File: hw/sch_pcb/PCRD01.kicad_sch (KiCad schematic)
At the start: 40 parts, among them J1 JUMP_3X2, J2 JUMP_5X2, J3 CONN1_2, J4 CONN1_2, J5 Out, P1 _, P2 _, P3 _, P4 _, Q1 BF862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

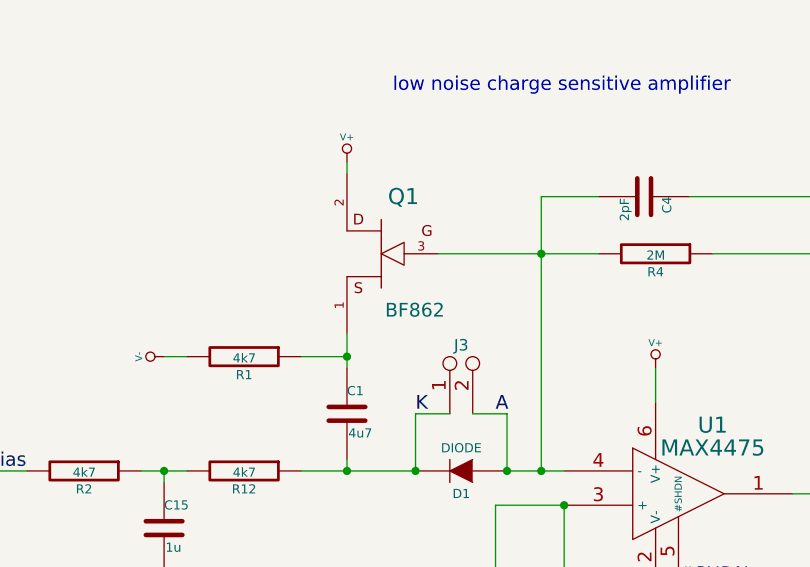
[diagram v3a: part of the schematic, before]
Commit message: replace PCB capacitor
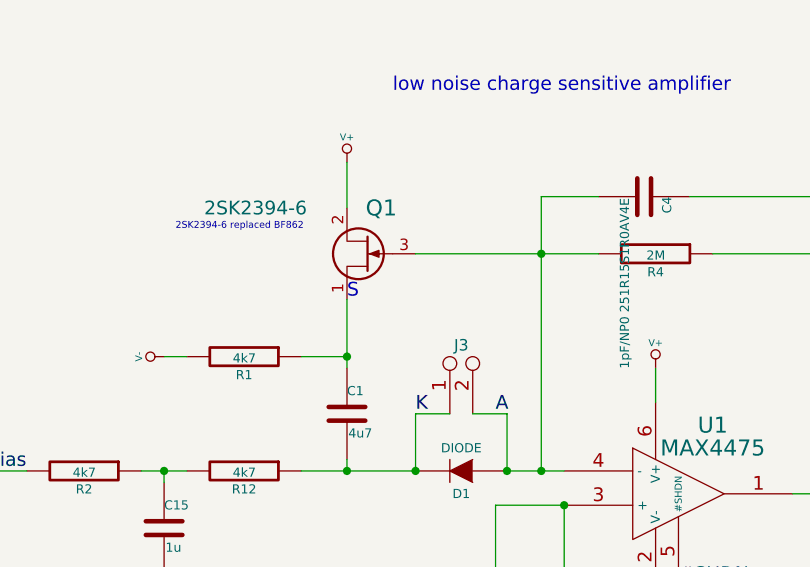
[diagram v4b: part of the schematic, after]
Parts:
- C4: value 2pF -> 1pF/NP0 251R15S1R0AV4E; footprint (none) -> Mlab_R:SMD-0805; UST_ID (none) -> 5c70984712875079b91f8b9f
- Q1: value BF862 -> 2SK2394-6; footprint MLAB_IO:SOT-23 -> Package_TO_SOT_SMD:SOT-23; symbol PCRD01A-rescue:JFET_N -> Transistor_FET:BF545A; UST_ID (none) -> 628d134fdc56076e9a223625
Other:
- note added: "2SK2394-6 replaced BF862"
- note added: "S"
- moved on the sheet: Q1
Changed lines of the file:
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@@
-    (stroke (width 0) (type default) (color 0 0 0 0))
-  )
-  (wire (pts (xy 63.5 67.31) (xy 63.5 66.04))
     (stroke (width 0) (type default) (color 0 0 0 0))
   )
@@
     (stroke (width 0) (type default) (color 0 0 0 0))
   )
-  (wire (pts (xy 73.66 76.2) (xy 85.09 76.2))
+  (wire (pts (xy 71.12 76.2) (xy 85.09 76.2))
     (stroke (width 0) (type default) (color 0 0 0 0))
   )
@@
     (stroke (width 0) (type default) (color 0 0 0 0))
   )
+  (wire (pts (xy 63.5 66.04) (xy 63.5 71.12))
+    (stroke (width 0) (type default) (color 0 0 0 0))
+  )
   (wire (pts (xy 58.42 87.63) (xy 63.5 87.63))
     (stroke (width 0) (type default) (color 0 0 0 0))
@@
     (stroke (width 0) (type default) (color 0 0 0 0))
   )
-  (wire (pts (xy 63.5 85.09) (xy 63.5 87.63))
+  (wire (pts (xy 63.5 81.28) (xy 63.5 87.63))
     (stroke (width 0) (type default) (color 0 0 0 0))
   )
@@
     (effects (font (size 1.524 1.524)) (justify left bottom))
   )
+  (text "S" (at 63.5 81.28 0)
+    (effects (font (size 1.524 1.524)) (justify left bottom))
+  )
   (text "+/- 2,4V" (at 38.1 154.94 0)
     (effects (font (size 1.524 1.524)) (justify left bottom))
@@
   (text "amplifier 7,7x" (at 152.4 86.36 0)
     (effects (font (size 1.524 1.524)) (justify left bottom))
+  )
+  (text "2SK2394-6 replaced BF862" (at 44.45 73.66 0)
+    (effects (font (size 0.762 0.762)) (justify left bottom))
   )
   (text "low noise charge sensitive amplifier" (at 68.58 58.42 0)
@@
     (pin "2")
   )
-  (symbol (lib_id "PCRD01A-rescue:JFET_N") (at 67.31 76.2 0) (mirror y) (unit 1)
-    (in_bom yes) (on_board yes)
-    (property "Reference" "Q1" (id 0) (at 69.7738 69.85 0)
+  (symbol (lib_id "Transistor_FET:BF545A") (at 66.04 76.2 0) (mirror y) (unit 1)
+    (in_bom yes) (on_board yes)
+    (property "Reference" "Q1" (id 0) (at 67.31 71.12 0)
       (effects (font (size 1.778 1.778)))
     )
-    (property "Value" "BF862" (id 1) (at 71.0438 82.4738 0)
-      (effects (font (size 1.524 1.524)))
-    )
-    (property "Footprint" "MLAB_IO:SOT-23" (id 2) (at 67.31 76.2 0)
-      (effects (font (size 1.524 1.524)) hide)
-    )
-    (property "Datasheet" "" (id 3) (at 67.31 76.2 0)
-      (effects (font (size 1.524 1.524)))
+    (property "Value" "2SK2394-6" (id 1) (at 53.34 71.12 0)
+      (effects (font (size 1.524 1.524)))
+    )
+    (property "Footprint" "Package_TO_SOT_SMD:SOT-23" (id 2) (at 60.96 78.105 0)
+      (effects (font (size 1.27 1.27) italic) (justify left) hide)
+    )
+    (property "Datasheet" "https://www.nxp.com/docs/en/data-sheet/BF545A_BF545B_BF545C.pdf" (id 3) (at 66.04 76.2 0)
+      (effects (font (size 1.27 1.27)) (justify left) hide)
+    )
+    (property "UST_ID" "628d134fdc56076e9a223625" (id 4) (at 66.04 76.2 0)
+      (effects (font (size 1.27 1.27)) hide)
     )
     (pin "1")
@@
       (effects (font (size 1.016 1.016)) (justify left))
     )
-    (property "Value" "2pF" (id 1) (at 94.361 70.0024 0)
-      (effects (font (size 1.016 1.016)) (justify left))
-    )
-    (property "Footprint" "" (id 2) (at 92.71 70.8152 0)
+    (property "Value" "1pF/NP0 251R15S1R0AV4E" (id 1) (at 94.361 70.0024 0)
+      (effects (font (size 1.016 1.016)) (justify left))
+    )
+    (property "Footprint" "Mlab_R:SMD-0805" (id 2) (at 92.71 70.8152 0)
       (effects (font (size 0.762 0.762)) hide)
     )
     (property "Datasheet" "" (id 3) (at 96.52 69.85 0)
       (effects (font (size 1.524 1.524)))
+    )
+    (property "UST_ID" "5c70984712875079b91f8b9f" (id 4) (at 96.52 69.85 0)
+      (effects (font (size 1.27 1.27)) hide)
     )
     (pin "1")
@@
     )
     (path "/00000000-0000-0000-0000-0000547638f8"
-      (reference "C4") (unit 1) (value "2pF") (footprint "")
+      (reference "C4") (unit 1) (value "1pF/NP0 251R15S1R0AV4E") (footprint "Mlab_R:SMD-0805")
     )
     (path "/00000000-0000-0000-0000-00005483ba04"
@@
     )
     (path "/00000000-0000-0000-0000-000054763801"
-      (reference "Q1") (unit 1) (value "BF862") (footprint "MLAB_IO:SOT-23")
+      (reference "Q1") (unit 1) (value "2SK2394-6") (footprint "Package_TO_SOT_SMD:SOT-23")
     )
     (path "/00000000-0000-0000-0000-0000547633b6"

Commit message: uklid layoutu
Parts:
- removed J3: CONN1_2, Hrebinky:CONN_3_2, symbol PCRD01A-rescue:CONN1_2
- added J3: HEADER_1x03, Mlab_Pin_Headers:Straight_1x03, symbol MLAB_HEADER:HEADER_1x03
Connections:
- net A: now also J3.3
- net GND: now also J3.2
- net K: now also J3.1
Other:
- note added: "Originaly: PCB 2pF capacitor"
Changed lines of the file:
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@@
     (stroke (width 0) (type default) (color 0 0 0 0))
   )
-  (wire (pts (xy 71.12 93.98) (xy 74.93 93.98))
+  (wire (pts (xy 71.12 93.98) (xy 73.66 93.98))
     (stroke (width 0) (type default) (color 0 0 0 0))
   )
@@
     (stroke (width 0) (type default) (color 0 0 0 0))
   )
+  (wire (pts (xy 78.74 93.98) (xy 81.28 93.98))
+    (stroke (width 0) (type default) (color 0 0 0 0))
+  )
   (wire (pts (xy 113.03 102.87) (xy 115.57 102.87))
     (stroke (width 0) (type default) (color 0 0 0 0))
@@
     (stroke (width 0) (type default) (color 0 0 0 0))
   )
+  (wire (pts (xy 73.66 88.9) (xy 73.66 93.98))
+    (stroke (width 0) (type default) (color 0 0 0 0))
+  )
   (wire (pts (xy 261.62 26.67) (xy 261.62 30.48))
     (stroke (width 0) (type default) (color 0 0 0 0))
@@
     (stroke (width 0) (type default) (color 0 0 0 0))
   )
-  (wire (pts (xy 77.47 93.98) (xy 81.28 93.98))
-    (stroke (width 0) (type default) (color 0 0 0 0))
-  )
   (wire (pts (xy 267.97 102.87) (xy 270.51 102.87))
     (stroke (width 0) (type default) (color 0 0 0 0))
@@
   )
   (wire (pts (xy 43.18 165.1) (xy 43.18 170.18))
+    (stroke (width 0) (type default) (color 0 0 0 0))
+  )
+  (wire (pts (xy 78.74 88.9) (xy 78.74 93.98))
     (stroke (width 0) (type default) (color 0 0 0 0))
   )
@@
   (text "amplifier 7,7x" (at 152.4 86.36 0)
     (effects (font (size 1.524 1.524)) (justify left bottom))
+  )
+  (text "Originaly: PCB 2pF capacitor" (at 90.17 64.77 0)
+    (effects (font (size 0.762 0.762)) (justify left bottom))
   )
   (text "2SK2394-6 replaced BF862" (at 44.45 73.66 0)
@@
       (effects (font (size 1.016 1.016)) (justify left))
     )
-    (property "Value" "1pF/NP0 251R15S1R0AV4E" (id 1) (at 94.361 70.0024 0)
+    (property "Value" "1pF/NP0 251R15S1R0AV4E" (id 1) (at 90.17 66.04 90)
       (effects (font (size 1.016 1.016)) (justify left))
     )
@@
     (pin "1")
   )
-  (symbol (lib_id "PCRD01A-rescue:CONN1_2") (at 76.2 86.36 90) (unit 1)
-    (in_bom yes) (on_board yes)
-    (property "Reference" "J3" (id 0) (at 76.2 86.36 90))
-    (property "Value" "CONN1_2" (id 1) (at 77.47 83.82 0)
-      (effects (font (size 1.016 1.016)) hide)
-    )
-    (property "Footprint" "Hrebinky:CONN_3_2" (id 2) (at 77.47 85.09 0)
+  (symbol (lib_id "PCRD01A-rescue:V+") (at 105.41 116.84 0) (unit 1)
+    (in_bom yes) (on_board yes)
+    (property "Reference" "#PWR031" (id 0) (at 105.41 114.3 0)
+      (effects (font (size 0.762 0.762)) hide)
+    )
+    (property "Value" "V+" (id 1) (at 105.41 114.046 0)
+      (effects (font (size 0.762 0.762)))
+    )
+    (property "Footprint" "" (id 2) (at 105.41 116.84 0)
+      (effects (font (size 1.524 1.524)))
+    )
+    (property "Datasheet" "" (id 3) (at 105.41 116.84 0)
+      (effects (font (size 1.524 1.524)))
+    )
+    (pin "1")
+  )
+  (symbol (lib_id "PCRD01A-rescue:R") (at 52.07 100.33 270) (unit 1)
+    (in_bom yes) (on_board yes)
+    (property "Reference" "R12" (id 0) (at 52.07 102.362 90)
+      (effects (font (size 1.016 1.016)))
+    )
+    (property "Value" "4k7" (id 1) (at 52.0954 100.5078 90)
+      (effects (font (size 1.016 1.016)))
+    )
+    (property "Footprint" "Mlab_R:SMD-0805" (id 2) (at 52.07 98.552 90)
+      (effects (font (size 0.762 0.762)) hide)
+    )
+    (property "Datasheet" "" (id 3) (at 52.07 100.33 0)
+      (effects (font (size 0.762 0.762)))
+    )
+    (property "UST_ID" "5c70984612875079b91f8995" (id 4) (at 52.07 100.33 0)
+      (effects (font (size 1.27 1.27)) hide)
+    )
+    (pin "1")
+    (pin "2")
+  )
+  (symbol (lib_id "PCRD01A-rescue:C") (at 43.18 106.68 0) (unit 1)
+    (in_bom yes) (on_board yes)
+    (property "Reference" "C15" (id 0) (at 43.18 104.14 0)
+      (effects (font (size 1.016 1.016)) (justify left))
+    )
+    (property "Value" "1u" (id 1) (at 43.3324 108.839 0)
+      (effects (font (size 1.016 1.016)) (justify left))
+    )
+    (property "Footprint" "Mlab_R:SMD-0805" (id 2) (at 44.1452 110.49 0)
+      (effects (font (size 0.762 0.762)) hide)
+    )
+    (property "Datasheet" "" (id 3) (at 43.18 106.68 0)
+      (effects (font (size 1.524 1.524)))
+    )
+    (property "UST_ID" "5c70984712875079b91f8b50" (id 4) (at 43.18 106.68 0)
+      (effects (font (size 1.27 1.27)) hide)
+    )
+    (pin "1")
+    (pin "2")
+  )
+  (symbol (lib_id "PCRD01A-rescue:GND") (at 43.18 113.03 0) (unit 1)
+    (in_bom yes) (on_board yes)
+    (property "Reference" "#PWR032" (id 0) (at 43.18 113.03 0)
+      (effects (font (size 0.762 0.762)) hide)
+    )
+    (property "Value" "GND" (id 1) (at 43.18 114.808 0)
+      (effects (font (size 0.762 0.762)) hide)
+    )
+    (property "Footprint" "" (id 2) (at 43.18 113.03 0)
+      (effects (font (size 1.524 1.524)))
+    )
+    (property "Datasheet" "" (id 3) (at 43.18 113.03 0)
+      (effects (font (size 1.524 1.524)))
+    )
+    (pin "1")
+  )
+  (symbol (lib_id "PCRD01A-rescue:GND") (at 76.2 88.9 0) (unit 1)
+    (in_bom yes) (on_board yes)
+    (property "Reference" "#PWR0101" (id 0) (at 76.2 88.9 0)
+      (effects (font (size 0.762 0.762)) hide)
+    )
+    (property "Value" "GND" (id 1) (at 76.2 90.678 0)
+      (effects (font (size 0.762 0.762)) hide)
+    )
+    (property "Footprint" "" (id 2) (at 76.2 88.9 0)
+      (effects (font (size 1.524 1.524)))
+    )
+    (property "Datasheet" "" (id 3) (at 76.2 88.9 0)
+      (effects (font (size 1.524 1.524)))
+    )
+    (pin "1")
+  )
+  (symbol (lib_id "MLAB_HEADER:HEADER_1x03") (at 76.2 83.82 90) (unit 1)
+    (in_bom yes) (on_board yes) (fields_autoplaced)
+    (property "Reference" "J3" (id 0) (at 81.28 84.455 90)
+      (effects (font (size 1.524 1.524)) (justify right))
+    )
+    (property "Value" "HEADER_1x03" (id 1) (at 81.28 86.36 90)
+      (effects (font (size 1.524 1.524)) (justify right) hide)
+    )
+    (property "Footprint" "Mlab_Pin_Headers:Straight_1x03" (id 2) (at 73.66 83.82 0)
       (effects (font (size 1.524 1.524)) hide)
     )
-    (property "Datasheet" "" (id 3) (at 77.47 85.09 0)
-      (effects (font (size 1.524 1.524)))
-    )
-    (pin "1")
-    (pin "2")
-  )
-  (symbol (lib_id "PCRD01A-rescue:V+") (at 105.41 116.84 0) (unit 1)
-    (in_bom yes) (on_board yes)
-    (property "Reference" "#PWR031" (id 0) (at 105.41 114.3 0)
-      (effects (font (size 0.762 0.762)) hide)
-    )
-    (property "Value" "V+" (id 1) (at 105.41 114.046 0)
-      (effects (font (size 0.762 0.762)))
-    )
-    (property "Footprint" "" (id 2) (at 105.41 116.84 0)
-      (effects (font (size 1.524 1.524)))
-    )
-    (property "Datasheet" "" (id 3) (at 105.41 116.84 0)
-      (effects (font (size 1.524 1.524)))
-    )
-    (pin "1")
-  )
-  (symbol (lib_id "PCRD01A-rescue:R") (at 52.07 100.33 270) (unit 1)
-    (in_bom yes) (on_board yes)
-    (property "Reference" "R12" (id 0) (at 52.07 102.362 90)
-      (effects (font (size 1.016 1.016)))
-    )
-    (property "Value" "4k7" (id 1) (at 52.0954 100.5078 90)
-      (effects (font (size 1.016 1.016)))
-    )
-    (property "Footprint" "Mlab_R:SMD-0805" (id 2) (at 52.07 98.552 90)
-      (effects (font (size 0.762 0.762)) hide)
-    )
-    (property "Datasheet" "" (id 3) (at 52.07 100.33 0)
-      (effects (font (size 0.762 0.762)))
-    )
-    (property "UST_ID" "5c70984612875079b91f8995" (id 4) (at 52.07 100.33 0)
-      (effects (font (size 1.27 1.27)) hide)
-    )
-    (pin "1")
-    (pin "2")
-  )
-  (symbol (lib_id "PCRD01A-rescue:C") (at 43.18 106.68 0) (unit 1)
-    (in_bom yes) (on_board yes)
-    (property "Reference" "C15" (id 0) (at 43.18 104.14 0)
-      (effects (font (size 1.016 1.016)) (justify left))
-    )
-    (property "Value" "1u" (id 1) (at 43.3324 108.839 0)
-      (effects (font (size 1.016 1.016)) (justify left))
-    )
-    (property "Footprint" "Mlab_R:SMD-0805" (id 2) (at 44.1452 110.49 0)
-      (effects (font (size 0.762 0.762)) hide)
-    )
-    (property "Datasheet" "" (id 3) (at 43.18 106.68 0)
-      (effects (font (size 1.524 1.524)))
-    )
-    (property "UST_ID" "5c70984712875079b91f8b50" (id 4) (at 43.18 106.68 0)
-      (effects (font (size 1.27 1.27)) hide)
-    )
-    (pin "1")
-    (pin "2")
-  )
-  (symbol (lib_id "PCRD01A-rescue:GND") (at 43.18 113.03 0) (unit 1)
-    (in_bom yes) (on_board yes)
-    (property "Reference" "#PWR032" (id 0) (at 43.18 113.03 0)
-      (effects (font (size 0.762 0.762)) hide)
-    )
-    (property "Value" "GND" (id 1) (at 43.18 114.808 0)
-      (effects (font (size 0.762 0.762)) hide)
-    )
-    (property "Footprint" "" (id 2) (at 43.18 113.03 0)
-      (effects (font (size 1.524 1.524)))
-    )
-    (property "Datasheet" "" (id 3) (at 43.18 113.03 0)
-      (effects (font (size 1.524 1.524)))
-    )
-    (pin "1")
+    (property "Datasheet" "" (id 3) (at 73.66 83.82 0)
+      (effects (font (size 1.524 1.524)))
+    )
+    (pin "1")
+    (pin "2")
+    (pin "3")
   )
   (sheet_instances
@@
       (reference "#PWR032") (unit 1) (value "GND") (footprint "")
     )
+    (path "/4c66d86a-55d0-4bc7-9f02-eebc8b70e762"
+      (reference "#PWR0101") (unit 1) (value "GND") (footprint "")
+    )
     (path "/00000000-0000-0000-0000-00005476354e"
       (reference "C1") (unit 1) (value "4u7") (footprint "Mlab_R:SMD-0805")
@@
       (reference "J2") (unit 1) (value "JUMP_5X2") (footprint "Hrebinky:Pin_Header_Straight_2x05")
     )
-    (path "/00000000-0000-0000-0000-0000548463a5"
-      (reference "J3") (unit 1) (value "CONN1_2") (footprint "Hrebinky:CONN_3_2")
+    (path "/bd4f2901-c4b7-4421-b66c-d0d47ad8871a"
+      (reference "J3") (unit 1) (value "HEADER_1x03") (footprint "Mlab_Pin_Headers:Straight_1x03")
     )
     (path "/00000000-0000-0000-0000-00005483ad5f"

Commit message: Edit PCB
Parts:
- C1, C10, C11, C12, C13, C15, C2, C3, C4, C5, C6, C7, C8, C9: footprint Mlab_R:SMD-0805 -> Capacitor_SMD:C_0805_2012Metric
- C14: footprint MLAB_R:SMD-0805 -> Capacitor_SMD:C_0805_2012Metric
- J1, J5: footprint Hrebinky:Pin_Header_Straight_2x03 -> Mlab_Pin_Headers:Straight_2x03; symbol PCRD01A-rescue:JUMP_3X2 -> MLAB_HEADER:HEADER_2x03_PARALLEL
- J2: footprint Hrebinky:Pin_Header_Straight_2x05 -> Mlab_Pin_Headers:Straight_2x05; symbol PCRD01A-rescue:JUMP_5X2 -> MLAB_HEADER:HEADER_2x05_PARALLEL
- J4: footprint Hrebinky:Pin_Header_Straight_1x02 -> Mlab_Pin_Headers:Straight_1x02
- R1, R10, R11, R12, R2, R3, R4, R5, R6, R7, R8, R9: footprint Mlab_R:SMD-0805 -> Resistor_SMD:R_0805_2012Metric
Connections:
- net +Ubias: now also J1.3, J1.4; no longer J1.2 (1), J1.5
- net GND: now also J1.2, J1.5, J2.2, J2.9, J5.2, J5.5; no longer J1.3, J1.4, J2.5, J2.6, J5.3, J5.4
- net V+: now also J2.5, J2.6; no longer J2.3, J2.8
- net V-: now also J2.3, J2.8; no longer J2.2, J2.9
- net at C14.2, R11.1: now also J5.3, J5.4; no longer J5.2 (1), J5.5
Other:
- moved on the sheet: C11, C12, C13, C14, C15, R1, R10, R11, R12, R2, R6, R7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
